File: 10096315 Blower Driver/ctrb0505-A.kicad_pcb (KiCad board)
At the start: 4 copper layers, 92.5 x 72 mm, 151 parts, among them IC1 L-BC-SO24, IC2 L-BC-SO08, IC3 L-BC-SO08, IC4 L-BC-SO08, IC5 L-BC-SO08, IC6 REG-BC-DPAK, J1 F-COCMS-MOL43650-0212, J11 F-CO-MOL5566-02, J2 F-CO-HE10-2010D, J22 F-CO-MOL7395M09, J3 F-CO-MOL7395M02, J4 JUMPER2_NoCopper, J6 F-CO-MOL7395M08, T1 Q-SOT23-IRLML2803, T10 Q-SOT23-IRLML2803, T2 Q-BC-DPAK-GDS, T3 Q-BC-DPAK-GDS, T4 Q-BC-DPAK-GDS, T5 Q-BC-DPAK-GDS, T6 Q-BC-DPAK-GDS, T7 Q-BC-DPAK-GDS, T8 Q-SOT23-IRLML2803, T9 Q-BC-DPAK-GDS

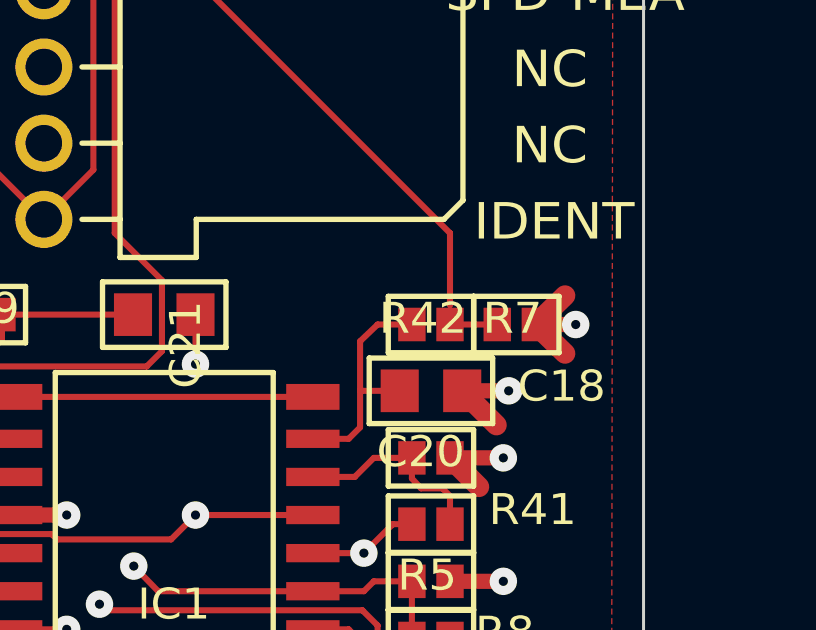
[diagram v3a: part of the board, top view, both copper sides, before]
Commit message: Layout Kicad: remove DRC due to unconnected track close to R42 on top layer
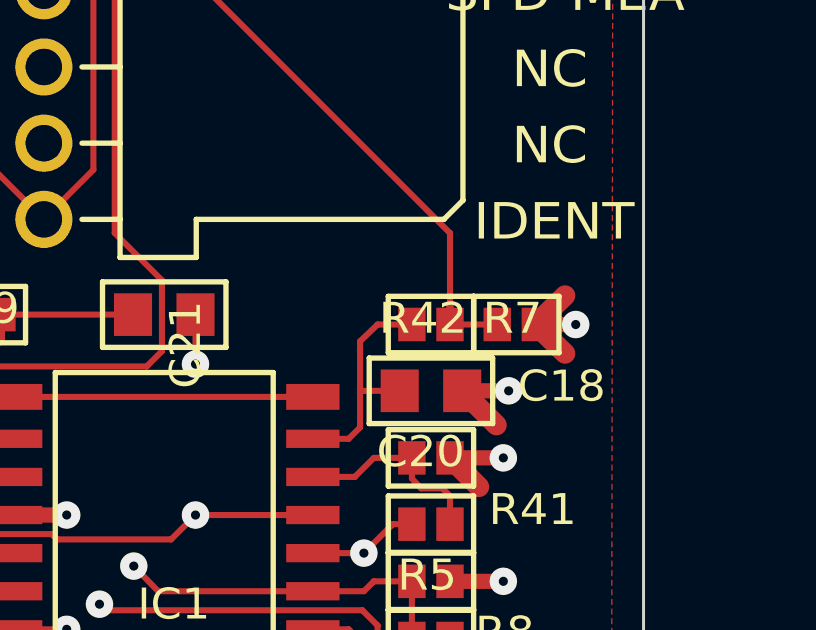
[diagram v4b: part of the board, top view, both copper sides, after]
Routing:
- net N12: track 30.4 -> 31.0 mm
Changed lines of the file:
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@@
     (thickness 1.6)
     (drawings 63)
-    (tracks 1110)
+    (tracks 1111)
     (zones 0)
     (modules 151)
@@
   (page A4)
   (layers
-    (0 F.Cu signal hide)
-    (1 In1.Cu signal hide)
+    (0 F.Cu signal)
+    (1 In1.Cu signal)
     (2 In2.Cu signal)
-    (31 B.Cu signal hide)
+    (31 B.Cu signal)
     (32 B.Adhes user)
     (33 F.Adhes user)
@@
     (solder_mask_min_width 0.25)
     (aux_axis_origin 0 0)
-    (visible_elements FFFEFF7F)
+    (visible_elements FFFFFF7F)
     (pcbplotparams
       (layerselection 0x010fc_ffffffff)
@@
   (segment (start 319.2448 61.3256) (end 319.2448 46.5936) (width 0.2032) (layer F.Cu) (net 37))
   (segment (start 327.4998 72.6286) (end 329.0746 72.6286) (width 0.2032) (layer F.Cu) (net 37))
+  (segment (start 327.4998 71.9936) (end 327.4998 72.6286) (width 0.25) (layer F.Cu) (net 37))
   (segment (start 268.1146 94.8536) (end 269.8926 94.8536) (width 0.2032) (layer F.Cu) (net 38))
   (via (at 266.8446 56.4996) (size 0.9144) (drill 0.3048) (layers F.Cu B.Cu) (net 39))

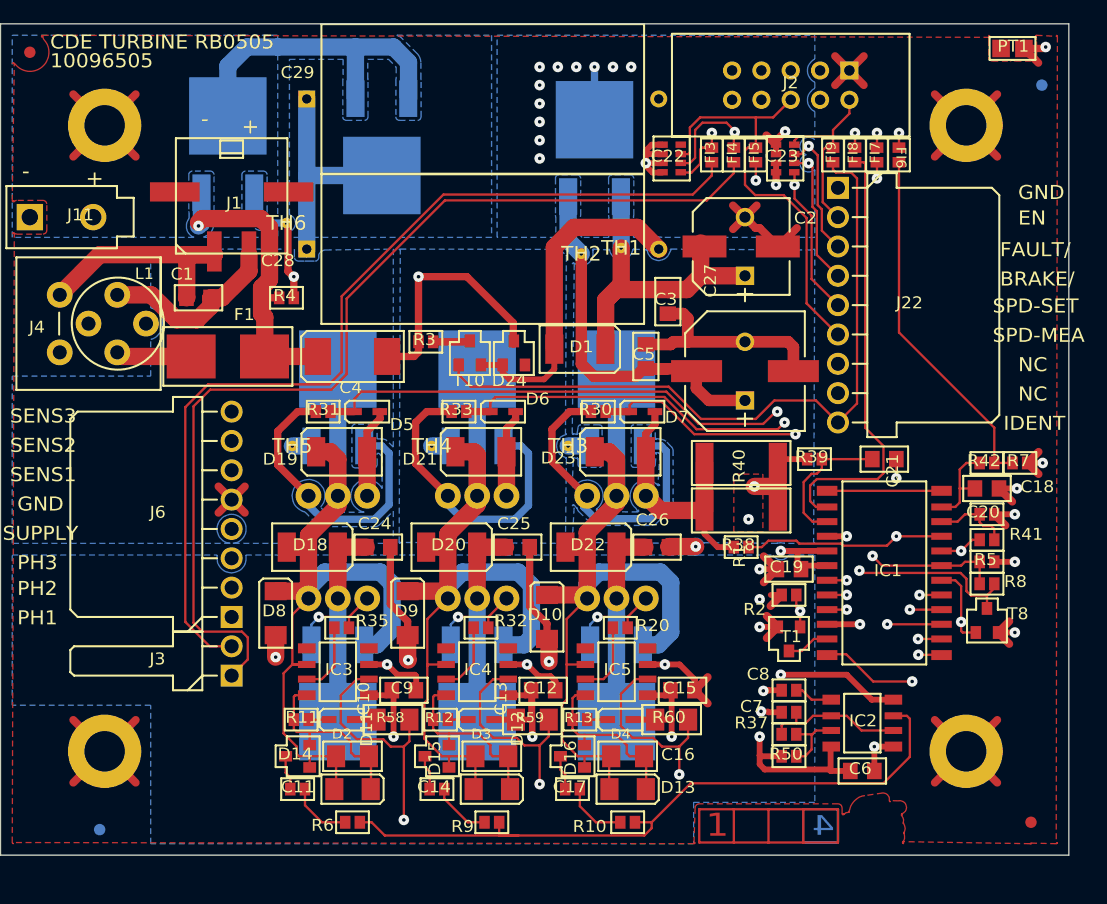
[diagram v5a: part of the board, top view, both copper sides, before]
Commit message: merge footprints of blower with cpu board
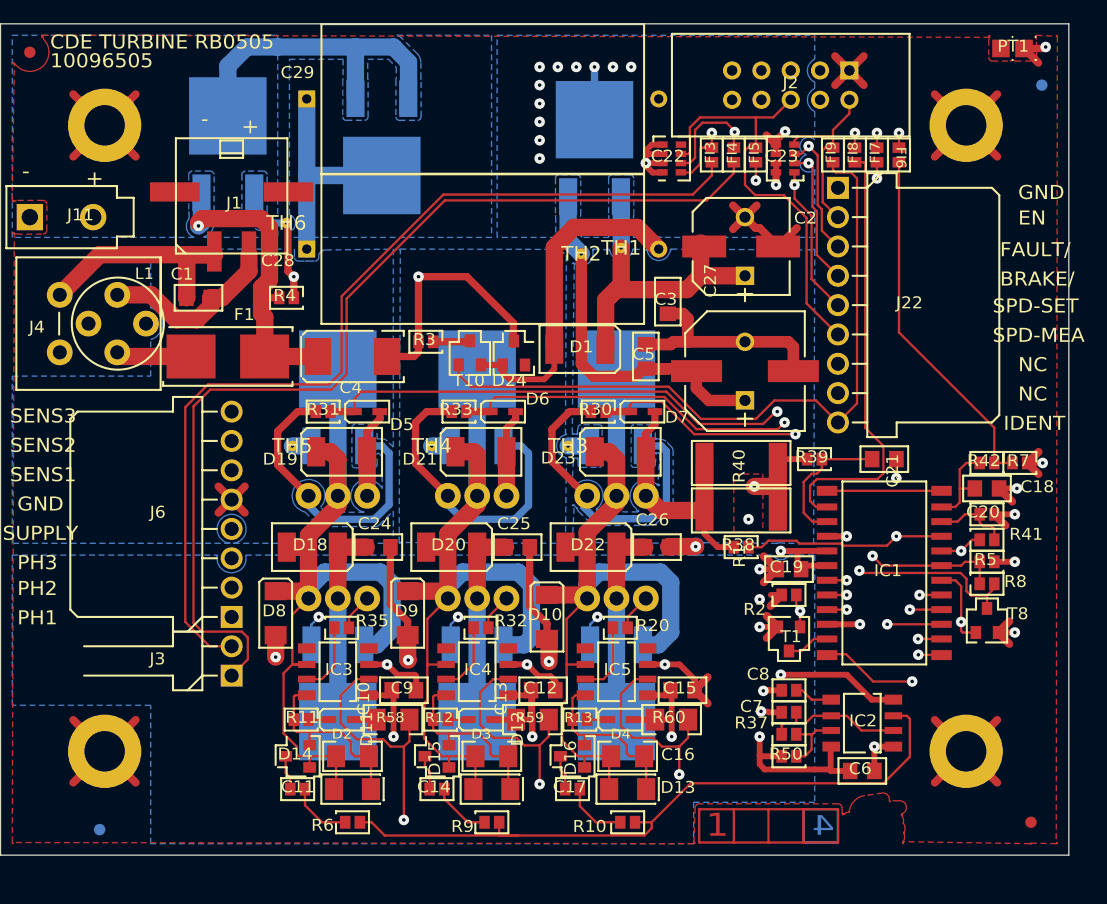
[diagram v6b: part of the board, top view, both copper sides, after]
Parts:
- C1, C12, C15, C18, C19, C21, C24, C25, C26, C3, C5, C6, C9: footprint ctrb0505-A:C0805_1 -> AllModules:C0805_1
- C10, C13, C16, R58, R59, R60: footprint ctrb0505-A:RC1206_1 -> AllModules:RC1206_1
- C11, C14, C17, C20, C7, C8, FI3, FI4, FI5, FI6, FI7, FI8, FI9: footprint ctrb0505-A:C0603_1 -> AllModules:C0603_1
- C2, C27: footprint ctrb0505-A:03515_1 -> AllModules:03515_1
- C22, C23: footprint ctrb0505-A:C0612-4_1 -> AllModules:C0612-4_1
- C28, C29: footprint ctrb0505-A:HT-13X27_1 -> AllModules:HT-13X27_1
- C4: footprint ctrb0505-A:C7343_1 -> AllModules:C7343_1
- CAM1, CAM2, CAM3, CAM4: footprint ctrb0505-A:COIN_EXTERNE_1 -> AllModules:COIN_EXTERNE_1
- CAM12: footprint ctrb0505-A:FABRICATION-FEE_1 -> AllModules:FABRICATION-FEE_1
- CAM13: footprint ctrb0505-A:PERCAGE_TABLEAU_1 -> AllModules:PERCAGE_TABLEAU_1
- CAM14: footprint ctrb0505-A:FEE_COMP_2 -> AllModules:FEE_COMP_2
- CAM15: footprint ctrb0505-A:FEE_COMP_1 -> AllModules:FEE_COMP_1
- CAM5: footprint ctrb0505-A:FILM18_HORIZONTAL_1 -> AllModules:FILM18_HORIZONTAL_1
- CAM6: footprint ctrb0505-A:A3_PER_COVIDIEN_1 -> AllModules:A3_PER_COVIDIEN_1
- CAM7: footprint ctrb0505-A:A3_EQFC_COVIDIEN_1 -> AllModules:A3_EQFC_COVIDIEN_1
- CAM8: footprint ctrb0505-A:PER-COVIDIEN_TEXTE_1 -> AllModules:PER-COVIDIEN_TEXTE_1
- CAM9: footprint ctrb0505-A:A3_EQFS_COVIDIEN_1 -> AllModules:A3_EQFS_COVIDIEN_1
- D1, D18, D19, D20, D21, D22, D23: footprint ctrb0505-A:SMB_1 -> AllModules:SMB_1
- D10, D8, D9: footprint ctrb0505-A:SMA_1 -> AllModules:SMA_1
- D11, D12, D13: footprint ctrb0505-A:SOD80_1 -> AllModules:SOD80_1
- D14, D15, D16, D24: footprint ctrb0505-A:SOT23-1G_1 -> AllModules:SOT23-1G_1
- D17: footprint ctrb0505-A:DPAK-2ANODES_1 -> AllModules:DPAK-2ANODES_1
- D2, D3, D4, D5, D6, D7: footprint ctrb0505-A:SOD323_1 -> AllModules:SOD323_1
- F1: footprint ctrb0505-A:FU154000_1 -> AllModules:FU154000_1
- FI1: footprint ctrb0505-A:BNX002_1 -> AllModules:BNX002_1
- IC1: footprint ctrb0505-A:MX.A24_COMPOSANT_1 -> AllModules:MX.A24_COMPOSANT_1
- IC2, IC3, IC4, IC5: footprint ctrb0505-A:MX.A8_COMPOSANT_1 -> AllModules:MX.A8_COMPOSANT_1
- IC6: footprint ctrb0505-A:DPAK_1 -> AllModules:DPAK_1b
- J1: footprint ctrb0505-A:MOL43650-02C_1 -> AllModules:MOL43650-02C_1
- J11: footprint ctrb0505-A:MOL5566-2_1 -> AllModules:MOL5566-2_1
- J2: footprint ctrb0505-A:BP2X5D_1 -> AllModules:BP2X5D_1
- J22: footprint ctrb0505-A:MOL7395-9_1 -> AllModules:MOL7395-9_1
- J3: footprint ctrb0505-A:MOL7395-2_1 -> AllModules:MOL7395-2_1
- J4: footprint ctrb0505-A:JUMPER2_NoCopper_1 -> AllModules:JUMPER2_NoCopper_1
- J6: footprint ctrb0505-A:MOL7395-8_1 -> AllModules:MOL7395-8_1
- L1: footprint ctrb0505-A:ELC09DxxxxF_NoCopper_1 -> AllModules:ELC09DxxxxF_NoCopper_1
- MIR1, MIR2, MIR3, MIR4: footprint ctrb0505-A:MIRECMS-SAFT_1 -> AllModules:MIRECMS-SAFT_1
- PT1: footprint ctrb0505-A:C12000_1 -> AllModules:C12000_1
- R1, R40: footprint ctrb0505-A:R2512_1 -> AllModules:R2512_1
- R10, R11, R12, R13, R2, R20, R3, R30, R31, R32, R33, R35, R37, R38, R39, R4, R41, R42, R5, R50, R6, R7, R8, R9: footprint ctrb0505-A:R0603_1 -> AllModules:R0603_1
- T1, T10, T8: footprint ctrb0505-A:SOT23-GSD_1 -> AllModules:SOT23-GSD_1
- T2, T3, T4, T5, T6, T7, T9: footprint ctrb0505-A:DPAK-GDS_1 -> AllModules:DPAK-GDS_1
- TH1, TH2, TH3, TH4, TH5, TH6: footprint ctrb0505-A:ThroughHole_36milx12mil_Pad_Cu_Mask -> AllModules:ThroughHole_36milx12mil_Pad_Cu_Mask
- ZC2: footprint ctrb0505-A:C-SC8_1 -> AllModules:C-SC8_1
- ZC27: footprint ctrb0505-A:C-SC10_1 -> AllModules:C-SC10_1
- ZM1, ZM2, ZM3, ZM4: footprint ctrb0505-A:FIX35M_1 -> AllModules:FIX35M_1
- ZT2, ZT3, ZT4, ZT5, ZT6, ZT7: footprint ctrb0505-A:TO220ABGDS-INV_COUCHE_1 -> AllModules:TO220ABGDS-INV_COUCHE_1
